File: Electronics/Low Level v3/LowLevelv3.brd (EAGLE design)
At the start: 117.3 x 68.1 mm, 53 parts, among them IC2 MCP4802, K1 ORWH-SH-105D1F,000, K3 ORWH-SH-105D1F,000, Q1 16MHz, T1 2N3904, T2 2N3904, U1 284512-4, U4 MCP2515, U5 MCP2551DIL08, X3 Motor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

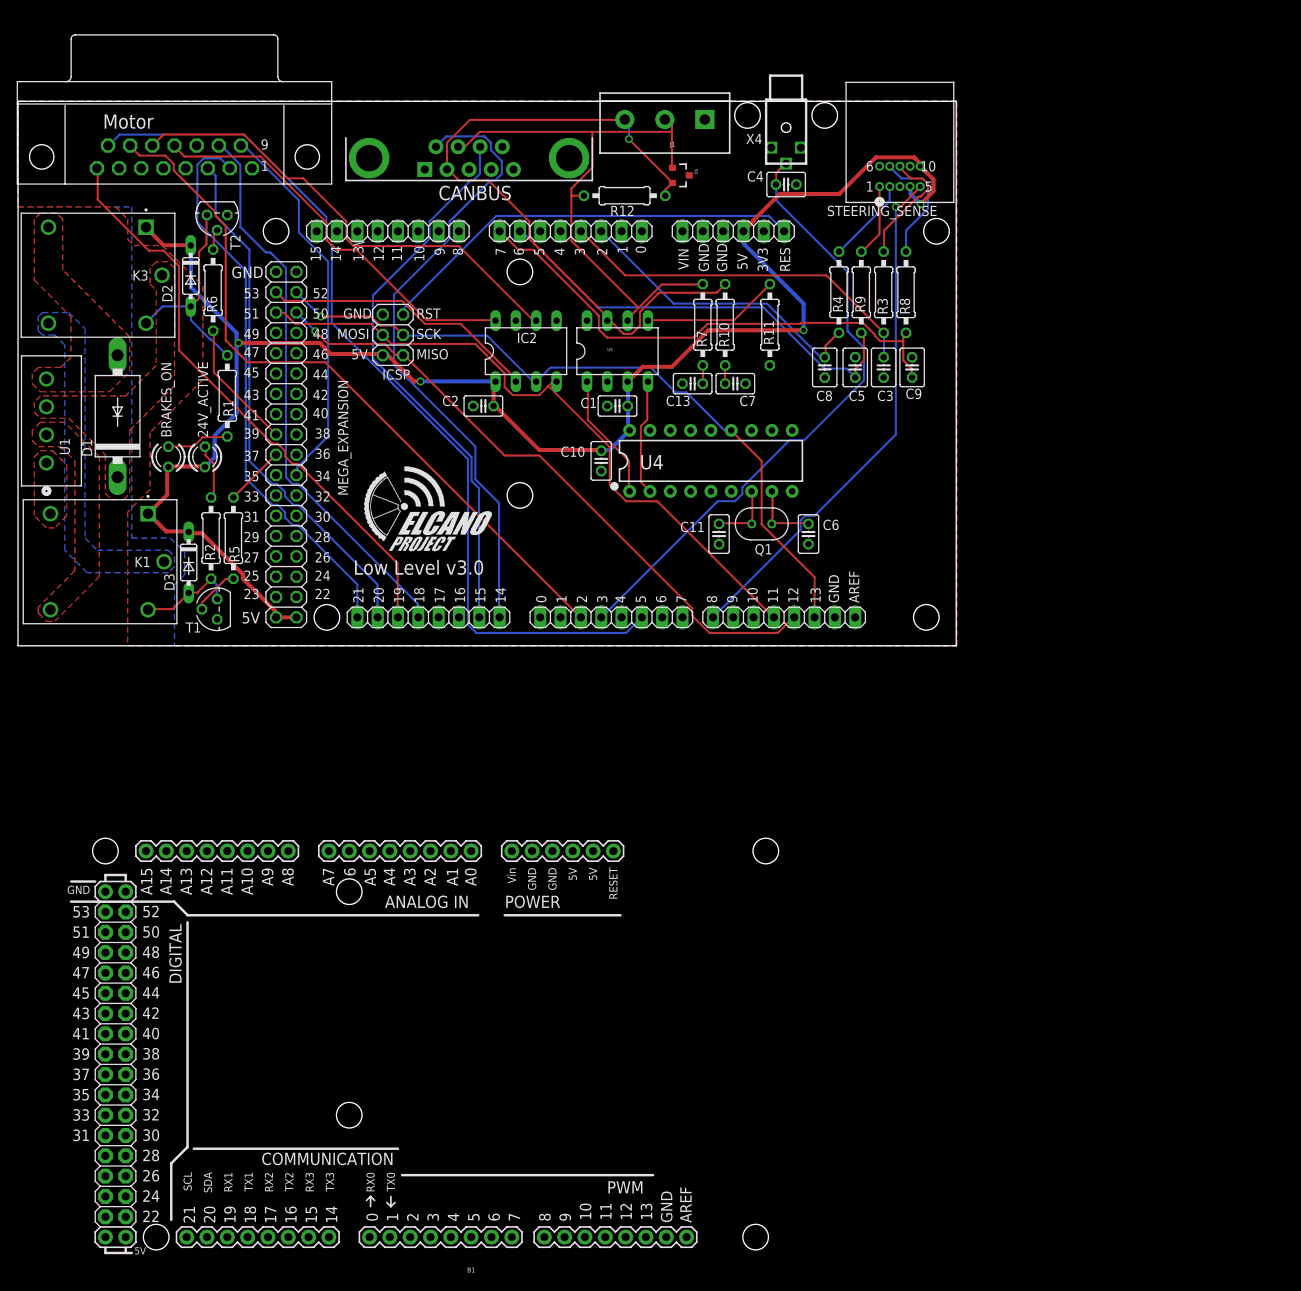
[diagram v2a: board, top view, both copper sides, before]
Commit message: removed accidental debugging Mega, added a handful of vias to fix GND orphans
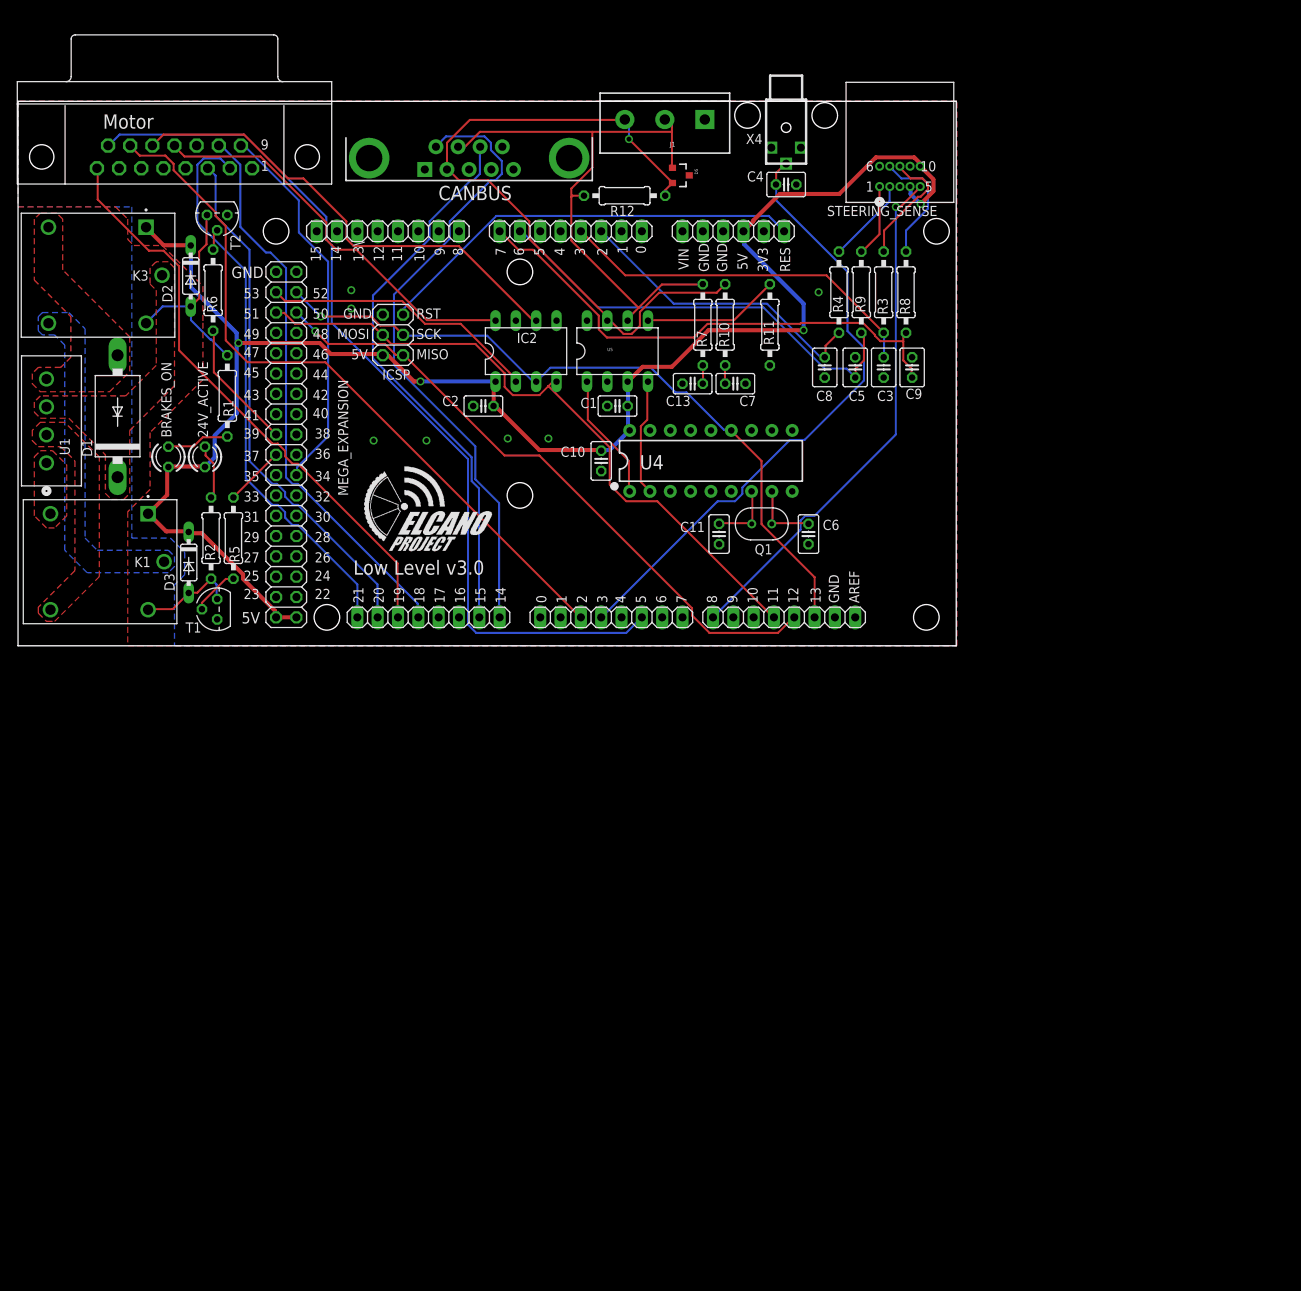
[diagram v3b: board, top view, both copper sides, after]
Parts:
- removed B1: ARDUINO_MEGA_R3FULL, SparkFun-Boards:ARDUINO_MEGA
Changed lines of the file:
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@@
 <attribute name="VALUE" x="77.3176" y="62.484" size="1.27" layer="27" ratio="10" rot="R180"/>
-</element>
-<element name="B1" library="SparkFun-Boards" library_urn="urn:adsk.eagle:library:509" package="ARDUINO_MEGA" package3d_urn="urn:adsk.eagle:package:37320/1" value="ARDUINO_MEGA_R3FULL" x="58.928" y="-44.196" smashed="yes" rot="R180">
-<attribute name="NAME" x="57.658" y="-72.136" size="0.6096" layer="25" font="vector" ratio="20" rot="R180" align="bottom-center"/>
-<attribute name="VALUE" x="58.928" y="-16.256" size="0.6096" layer="27" font="vector" ratio="20" rot="R180" align="top-center"/>
 </element>
 </elements>
@@
 </polygon>
 <contactref element="STEERING_SENSE" pad="6"/>
-<wire x1="27.178" y1="59.436" x2="23.3426" y2="68.1203" width="0" layer="19" extent="1-1"/>
-<wire x1="46.609" y1="46.99" x2="35.814" y2="52.324" width="0" layer="19" extent="1-1"/>
+<via x="42.672" y="47.752" extent="1-16" drill="0.6096"/>
+<via x="42.672" y="50.038" extent="1-16" drill="0.6096"/>
+<via x="45.466" y="31.242" extent="1-16" drill="0.6096"/>
+<via x="52.07" y="31.242" extent="1-16" drill="0.6096"/>
+<via x="62.23" y="31.496" extent="1-16" drill="0.6096"/>
+<via x="67.31" y="31.496" extent="1-16" drill="0.6096"/>
+<via x="101.092" y="49.784" extent="1-16" drill="0.6096"/>
 </signal>
 <signal name="RESET">

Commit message: schematic cleanup
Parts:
- DIGITAL_14-21: value DIG 14-21 -> Digital 14-21
- DIGITAL_8-13: value PWMH -> Digital 8-13
- MEGA_EXPANSION: value D22-D53 -> Digital 22-53
- renumbered COMM_DIG to DIGITAL_14-21, D8-13 to DIGITAL_8-13, PWML to DIGITAL_0-7
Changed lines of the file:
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@@
 <attribute name="VALUE" x="105.156" y="34.29" size="1.27" layer="27" ratio="10"/>
 </element>
-<element name="COMM_DIG" library="pinhead" library_urn="urn:adsk.eagle:library:325" package="1X08" package3d_urn="urn:adsk.eagle:package:22409/2" value="DIG 14-21" x="52.324" y="9.144" smashed="yes"/>
+<element name="DIGITAL_14-21" library="pinhead" library_urn="urn:adsk.eagle:library:325" package="1X08" package3d_urn="urn:adsk.eagle:package:22409/2" value="Digital 14-21" x="52.324" y="9.144" smashed="yes"/>
 <element name="IC2" library="ic-package" package="DIL08" value="MCP4802" x="64.516" y="42.418" smashed="yes">
 <attribute name="NAME" x="65.913" y="44.704" size="1.27" layer="25" ratio="10" rot="R180"/>
@@
 </element>
 <element name="POWER" library="pinhead" library_urn="urn:adsk.eagle:library:325" package="1X06" package3d_urn="urn:adsk.eagle:package:22472/2" value="" x="90.424" y="57.404" smashed="yes" rot="R180"/>
-<element name="PWML" library="pinhead" library_urn="urn:adsk.eagle:library:325" package="1X08" package3d_urn="urn:adsk.eagle:package:22409/2" value="Digital 0-7" x="75.184" y="9.144" smashed="yes"/>
+<element name="DIGITAL_0-7" library="pinhead" library_urn="urn:adsk.eagle:library:325" package="1X08" package3d_urn="urn:adsk.eagle:package:22409/2" value="Digital 0-7" x="75.184" y="9.144" smashed="yes"/>
 <element name="R3" library="rcl" library_urn="urn:adsk.eagle:library:334" package="0207/10" package3d_urn="urn:adsk.eagle:package:23491/2" value="4.7 K" x="109.22" y="49.784" smashed="yes" rot="R90">
 <attribute name="NAME" x="109.728" y="46.99" size="1.27" layer="25" ratio="10" rot="R90"/>
@@
 <attribute name="VALUE" x="105.156" y="34.29" size="1.27" layer="27" ratio="10"/>
 </element>
-<element name="D8-13" library="pinhead" library_urn="urn:adsk.eagle:library:325" package="1X08" package3d_urn="urn:adsk.eagle:package:22409/2" value="PWMH" x="96.774" y="9.144" smashed="yes"/>
+<element name="DIGITAL_8-13" library="pinhead" library_urn="urn:adsk.eagle:library:325" package="1X08" package3d_urn="urn:adsk.eagle:package:22409/2" value="Digital 8-13" x="96.774" y="9.144" smashed="yes"/>
 <element name="U4" library="SparkFun-IC-Comms" library_urn="urn:adsk.eagle:library:521" package="DIP18" package3d_urn="urn:adsk.eagle:package:38724/1" value=" MCP2515" x="87.63" y="28.702" smashed="yes">
 <attribute name="NAME" x="78.74" y="27.6479" size="1.778" layer="25" ratio="10"/>
@@
 <attribute name="VALUE" x="83.6295" y="65.405" size="0.4064" layer="27" rot="R270"/>
 </element>
-<element name="MEGA_EXPANSION" library="elcanoParts" package="PINHEAD_2X18" value="D22-D53" x="34.544" y="30.734" smashed="yes" rot="R270">
+<element name="MEGA_EXPANSION" library="elcanoParts" package="PINHEAD_2X18" value="Digital 22-53" x="34.544" y="30.734" smashed="yes" rot="R270">
 <attribute name="NAME" x="41.021" y="38.862" size="1.27" layer="25" ratio="10" rot="R270"/>
 <attribute name="VALUE" x="42.799" y="38.862" size="1.27" layer="27" rot="R270"/>
@@
 <signal name="SPEEDOMETER">
 <contactref element="X3" pad="14"/>
-<contactref element="PWML" pad="3"/>
+<contactref element="DIGITAL_0-7" pad="3"/>
 <wire x1="39.4335" y1="41.0337" x2="71.3232" y2="9.144" width="0.254" layer="1"/>
 <wire x1="29.718" y1="41.0337" x2="39.4335" y2="41.0337" width="0.254" layer="1"/>
@@
 </signal>
 <signal name="HALLPHASEB">
-<contactref element="COMM_DIG" pad="2"/>
+<contactref element="DIGITAL_14-21" pad="2"/>
 <contactref element="X3" pad="3"/>
 <wire x1="45.9486" y1="13.2588" x2="45.9486" y2="9.144" width="0.254" layer="16"/>
@@
 <signal name="WATCHDOG">
 <contactref element="X3" pad="15"/>
-<contactref element="PWML" pad="6"/>
+<contactref element="DIGITAL_0-7" pad="6"/>
 <wire x1="77.0382" y1="7.2009" x2="78.9813" y2="9.144" width="0.254" layer="16"/>
 <wire x1="58.293" y1="7.2009" x2="77.0382" y2="7.2009" width="0.254" layer="16"/>
@@
 </signal>
 <signal name="WHEELROTATION">
-<contactref element="PWML" pad="4"/>
+<contactref element="DIGITAL_0-7" pad="4"/>
 <contactref element="C4" pad="1"/>
 <contactref element="X4" pad="P$1"/>
@@
 <contactref element="U4" pad="13"/>
 <contactref element="IC2" pad="3"/>
-<contactref element="D8-13" pad="6"/>
+<contactref element="DIGITAL_8-13" pad="6"/>
 <contactref element="MEGA_EXPANSION" pad="4"/>
 <wire x1="100.584" y1="14.1732" x2="100.584" y2="9.144" width="0.254" layer="1"/>
@@
 <signal name="3MISO" class="3">
 <contactref element="ICSP" pad="1"/>
-<contactref element="D8-13" pad="5"/>
+<contactref element="DIGITAL_8-13" pad="5"/>
 <contactref element="MEGA_EXPANSION" pad="6"/>
 <wire x1="48.2346" y1="41.9481" x2="49.149" y2="41.9481" width="0.254" layer="1"/>
@@
 <signal name="3MOSI" class="3">
 <contactref element="ICSP" pad="4"/>
-<contactref element="D8-13" pad="4"/>
+<contactref element="DIGITAL_8-13" pad="4"/>
 <contactref element="IC2" pad="4"/>
 <contactref element="MEGA_EXPANSION" pad="5"/>
@@
 </signal>
 <signal name="HALLPHASEA">
-<contactref element="COMM_DIG" pad="1"/>
+<contactref element="DIGITAL_14-21" pad="1"/>
 <contactref element="X3" pad="2"/>
 <wire x1="43.434" y1="13.2588" x2="43.434" y2="9.144" width="0.254" layer="16"/>
@@
 </signal>
 <signal name="HALLPHASEC">
-<contactref element="COMM_DIG" pad="3"/>
+<contactref element="DIGITAL_14-21" pad="3"/>
 <contactref element="X3" pad="8"/>
 <wire x1="48.4632" y1="15.8877" x2="48.4632" y2="9.144" width="0.254" layer="1"/>
@@
 </signal>
 <signal name="EBIKECONTRL">
-<contactref element="COMM_DIG" pad="4"/>
+<contactref element="DIGITAL_14-21" pad="4"/>
 <contactref element="X3" pad="10"/>
 <wire x1="50.9778" y1="10.8585" x2="50.9778" y2="9.144" width="0.254" layer="16"/>
@@
 </signal>
 <signal name="TX3">
-<contactref element="COMM_DIG" pad="8"/>
+<contactref element="DIGITAL_14-21" pad="8"/>
 <contactref element="CANBUS" pad="6"/>
 <wire x1="61.1505" y1="23.4315" x2="61.1505" y2="9.144" width="0.254" layer="16"/>
@@
 </signal>
 <signal name="RX3">
-<contactref element="COMM_DIG" pad="7"/>
+<contactref element="DIGITAL_14-21" pad="7"/>
 <contactref element="CANBUS" pad="8"/>
 <wire x1="58.6359" y1="25.2603" x2="58.6359" y2="9.144" width="0.254" layer="16"/>
@@
 </signal>
 <signal name="STEER_SERVO_PWM">
-<contactref element="D8-13" pad="1"/>
+<contactref element="DIGITAL_8-13" pad="1"/>
 <contactref element="STEERING_SENSE" pad="5"/>
 <wire x1="110.744" y1="32.004" x2="110.744" y2="60.452" width="0.254" layer="16"/>

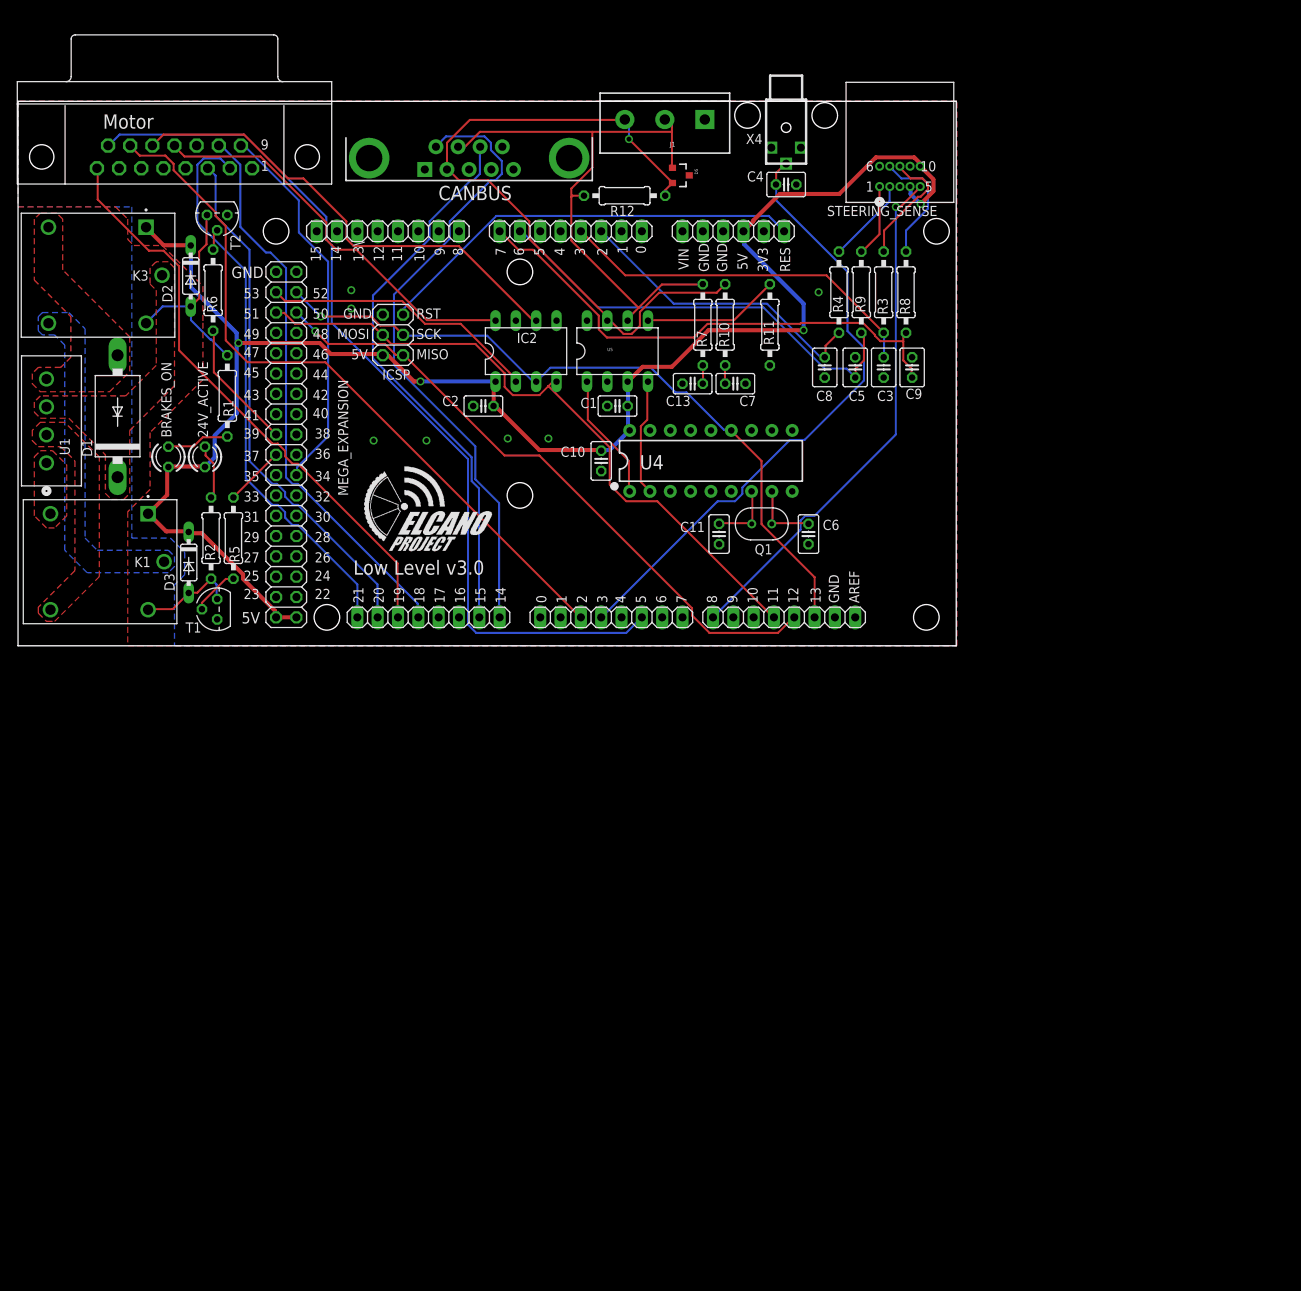
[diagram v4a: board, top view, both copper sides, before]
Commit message: rearranged silkscreen for clarity in v3
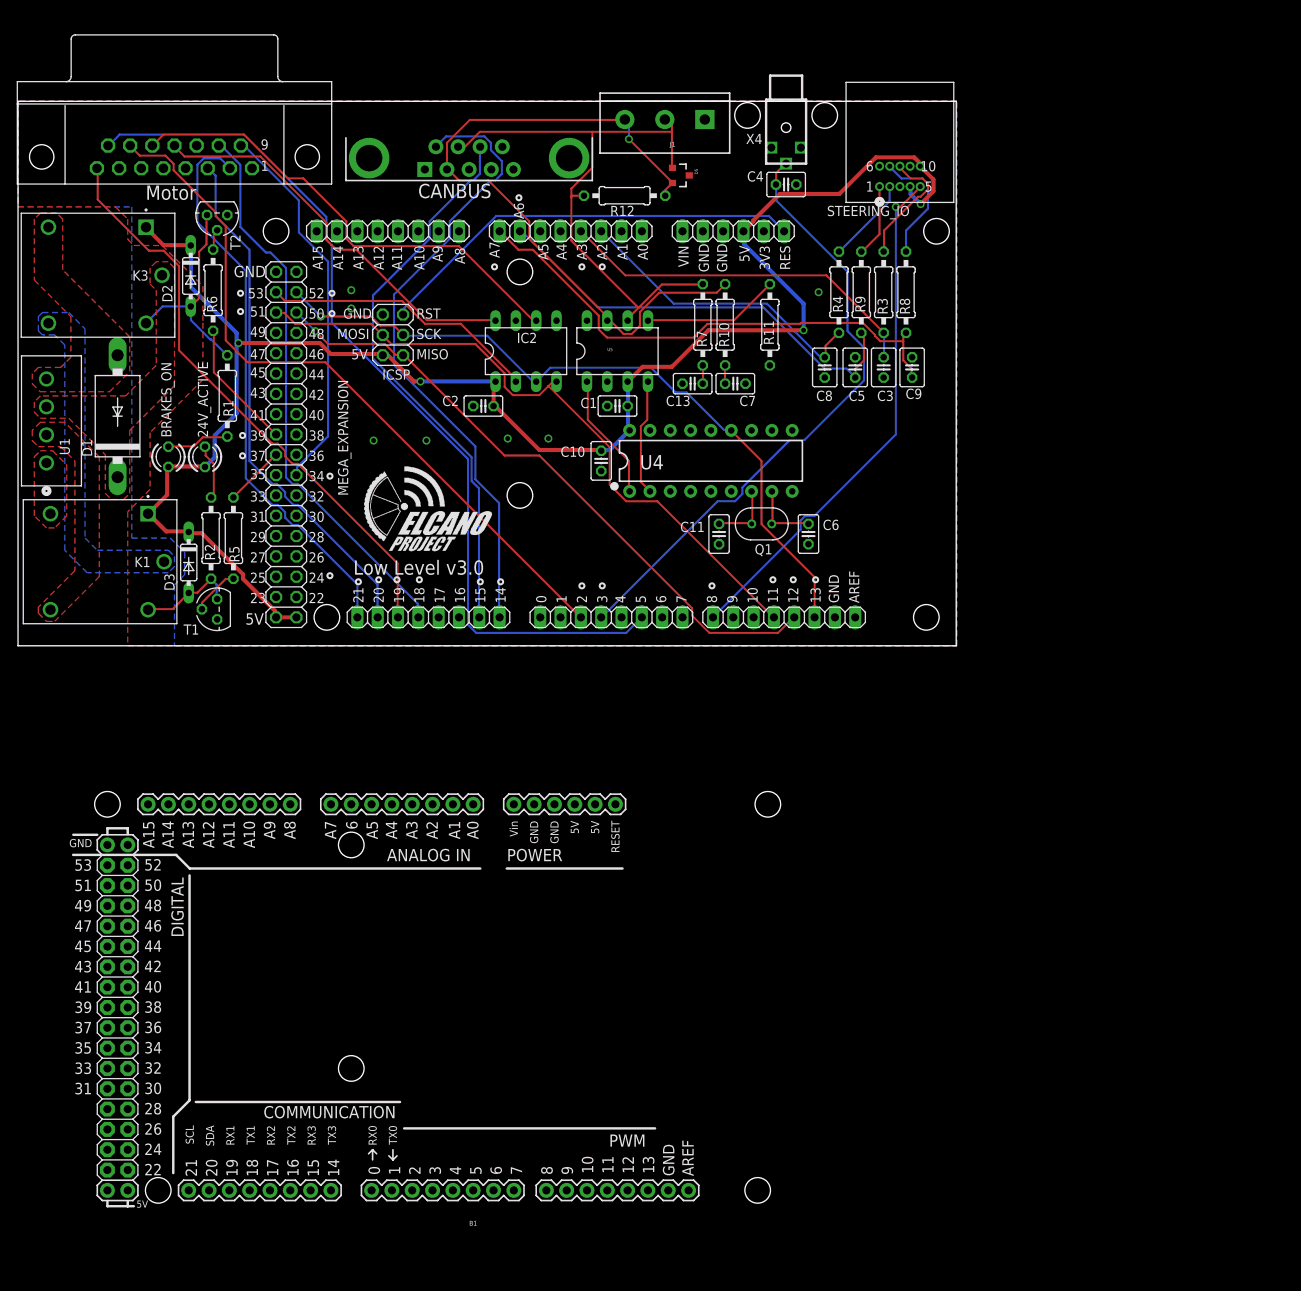
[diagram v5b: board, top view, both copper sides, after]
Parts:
- added B1: ARDUINO_MEGA_R3FULL, SparkFun-Boards:ARDUINO_MEGA
- renumbered STEERING_SENSE to STEERING_IO
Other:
- board text added: "A0"
- board text added: "A1"
- board text added: "A10"
- board text added: "A11"
- board text added: "A12"
- board text added: "A13"
- board text added: "A14"
- board text added: "A15"
- board text added: "A2"
- board text added: "A3"
- board text added: "A4"
- board text added: "A5"
- board text added: "A6"
- board text added: "A7"
- board text added: "A8"
- board text added: "A9"
- board text removed: "13\"
